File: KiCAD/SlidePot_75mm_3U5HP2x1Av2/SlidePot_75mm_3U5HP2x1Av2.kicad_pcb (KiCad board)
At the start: 2 copper layers, 25.1 x 128.5 mm, 4 parts

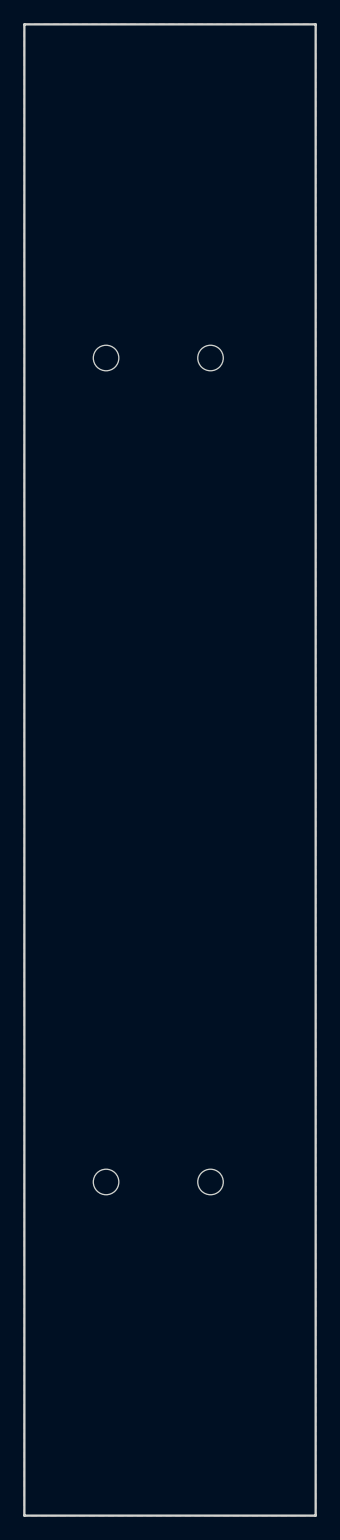
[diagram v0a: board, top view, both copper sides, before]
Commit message: updated all modules to use plated through-holes wherever possible
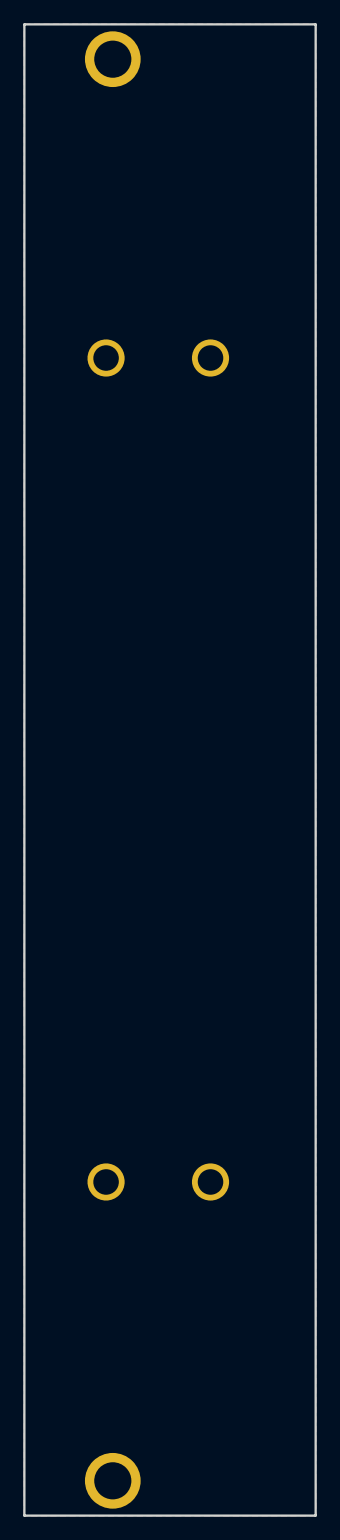
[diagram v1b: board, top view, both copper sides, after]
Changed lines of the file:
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@@
 			)
 		)
-		(pad "" np_thru_hole circle
+		(pad "" thru_hole circle
 			(at 0 -35.5)
-			(size 2.2 2.2)
+			(size 3.2 3.2)
 			(drill 2.2)
 			(layers "*.Cu" "*.Mask")
+			(remove_unused_layers no)
 		)
 		(pad "" np_thru_hole oval
@@
 			(layers "*.Cu" "*.Mask")
 		)
-		(pad "" np_thru_hole circle
+		(pad "" thru_hole circle
 			(at 0 35.5)
-			(size 2.2 2.2)
+			(size 3.2 3.2)
 			(drill 2.2)
 			(layers "*.Cu" "*.Mask")
+			(remove_unused_layers no)
 		)
 		(embedded_fonts no)
@@
 			)
 		)
-		(pad "" np_thru_hole oval
+		(pad "" thru_hole circle
 			(at 0 0)
-			(size 4.34 3.2)
-			(drill oval 4.34 3.2)
-			(layers "*.Cu" "*.Mask")
+			(size 4.8 4.8)
+			(drill 3.2)
+			(layers "*.Cu" "*.Mask")
+			(remove_unused_layers no)
 		)
 		(embedded_fonts no)
@@
 			)
 		)
-		(pad "" np_thru_hole oval
+		(pad "" thru_hole circle
 			(at 0 0)
-			(size 4.34 3.2)
-			(drill oval 4.34 3.2)
-			(layers "*.Cu" "*.Mask")
+			(size 4.8 4.8)
+			(drill 3.2)
+			(layers "*.Cu" "*.Mask")
+			(remove_unused_layers no)
 		)
 		(embedded_fonts no)
@@
 			)
 		)
-		(pad "" np_thru_hole circle
+		(pad "" thru_hole circle
 			(at 0 -35.5)
-			(size 2.2 2.2)
+			(size 3.2 3.2)
 			(drill 2.2)
 			(layers "*.Cu" "*.Mask")
+			(remove_unused_layers no)
 		)
 		(pad "" np_thru_hole oval
@@
 			(layers "*.Cu" "*.Mask")
 		)
-		(pad "" np_thru_hole circle
+		(pad "" thru_hole circle
 			(at 0 35.5)
-			(size 2.2 2.2)
+			(size 3.2 3.2)
 			(drill 2.2)
 			(layers "*.Cu" "*.Mask")
+			(remove_unused_layers no)
 		)
 		(embedded_fonts no)

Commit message: adjusted positioning of the slide pots in 3u5hp2x1 to fix tolerance issues
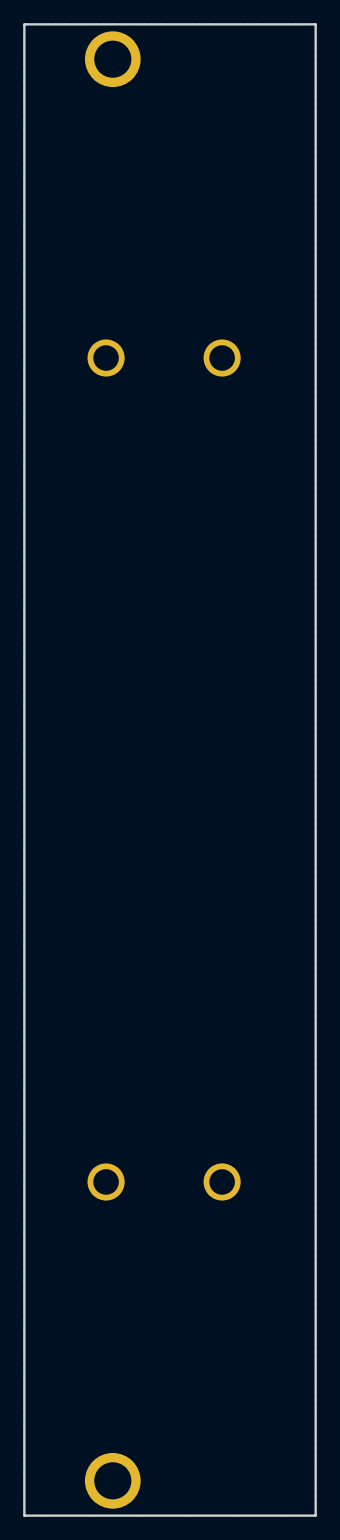
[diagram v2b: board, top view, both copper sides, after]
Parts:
- moved LP2 1.00 mm to (17.0, 66.7)
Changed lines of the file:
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@@
 	(footprint "EXC:Linear_Potentiometer_75mm_M2_Panel_Mount"
 		(layer "F.Cu")
-		(at 16.04 66.675)
+		(at 17.04 66.675)
 		(property "Reference" "LP2"
 			(at 0 -39.5 0)
